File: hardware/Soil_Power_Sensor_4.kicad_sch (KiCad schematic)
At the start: 14 parts, among them J6 UART, SW1 EN, SW2 BOOT, U9 ESP32-C3-WROOM-02-N4

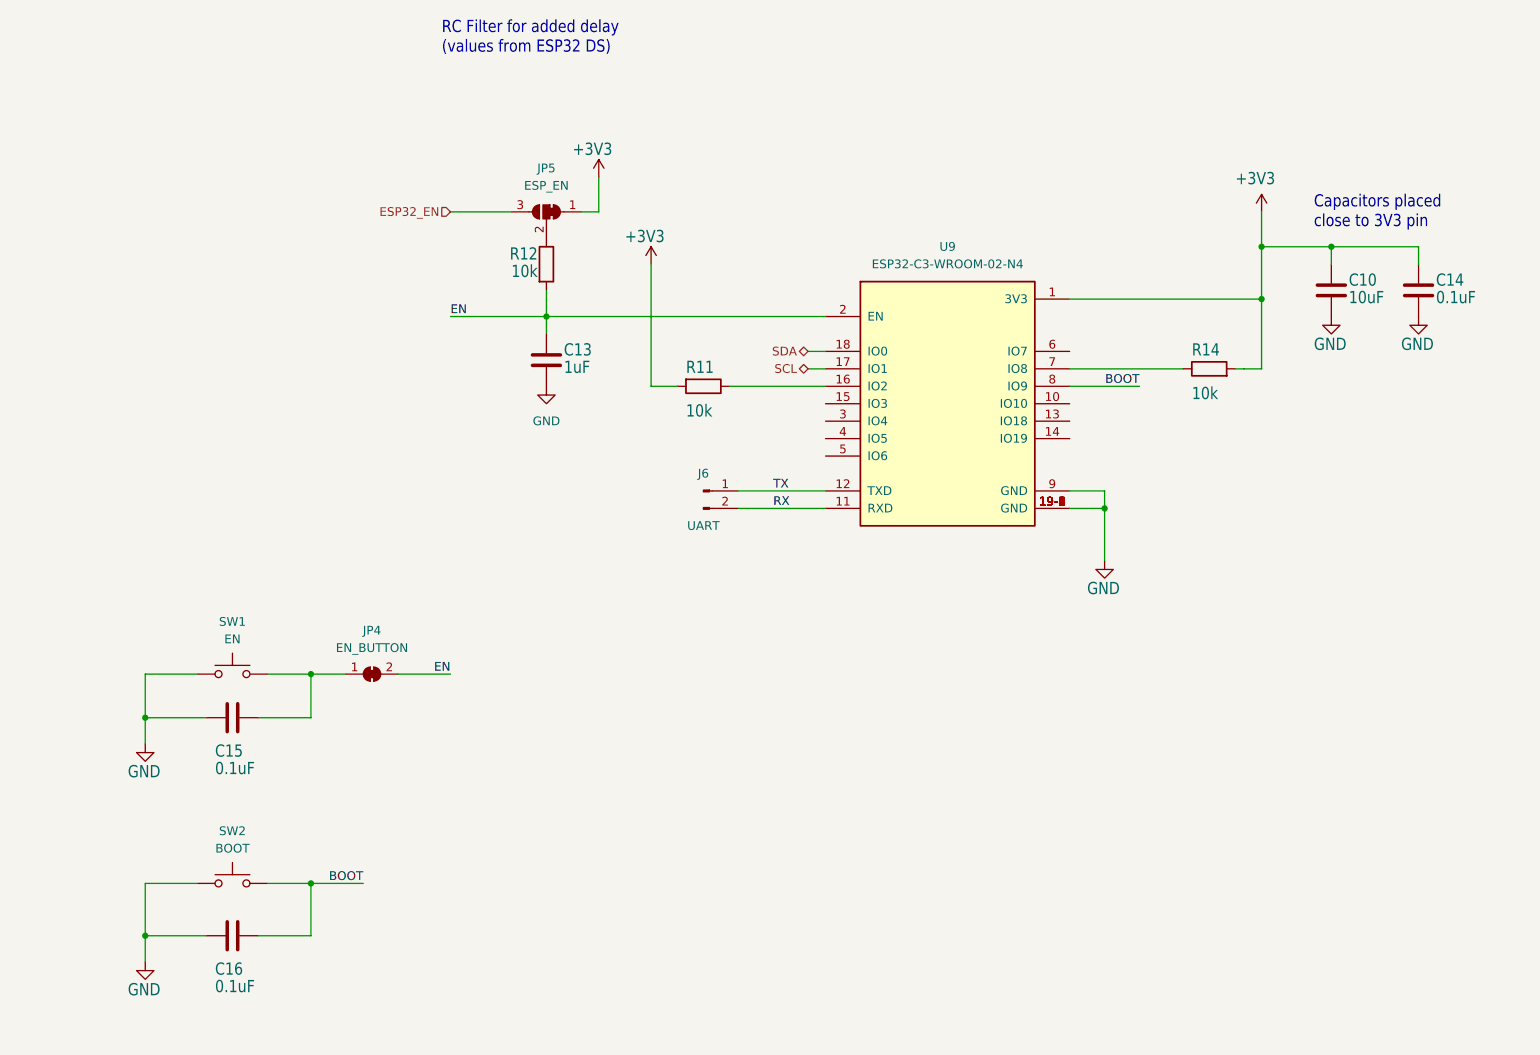
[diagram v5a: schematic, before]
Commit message: Updated annotations based on PCB position
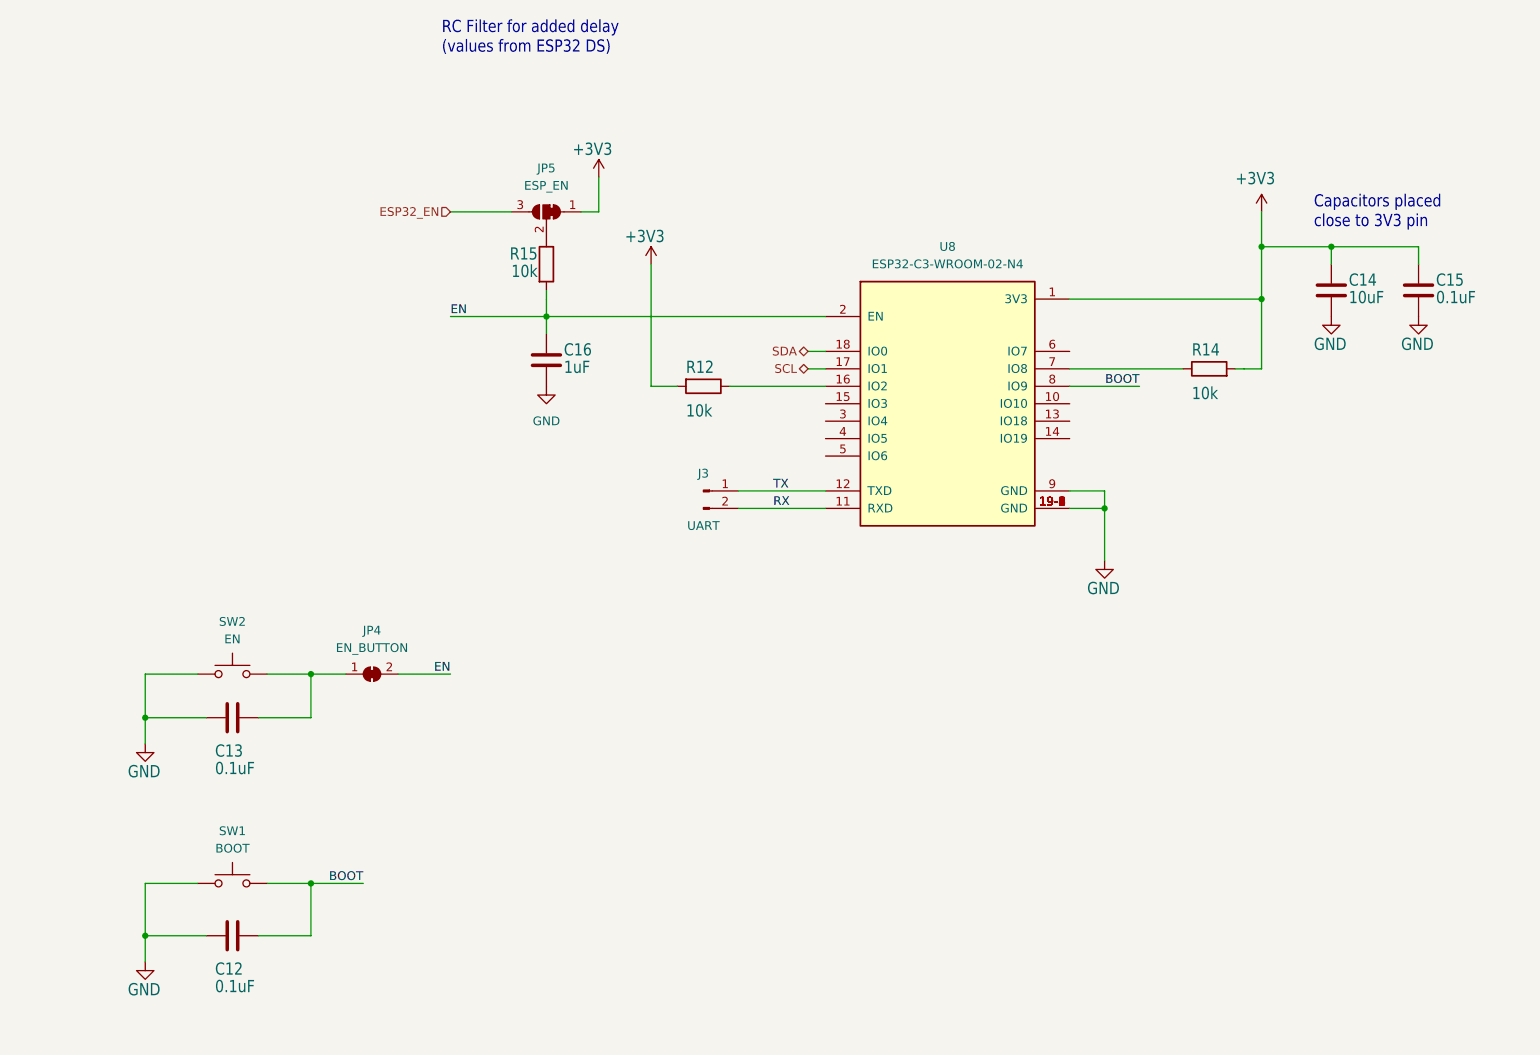
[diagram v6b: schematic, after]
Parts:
- renumbered C16 to C12, C15 to C13, C10 to C14, C14 to C15, C13 to C16, J6 to J3, R11 to R12, R12 to R15, SW2 to SW1, SW1 to SW2, U9 to U8
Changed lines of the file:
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@@
   (title_block
     (title "Soil Power Sensor")
-    (date "2023-10-09")
-    (rev "2.1.0")
+    (date "2024-03-08")
+    (rev "2.2.0")
     (company "jlab")
   )
@@
   (symbol (lib_id "Device:R") (at 129.54 88.9 270) (unit 1)
     (in_bom yes) (on_board yes) (dnp no)
-    (property "Reference" "R11" (at 127 85.09 90)
+    (property "Reference" "R12" (at 127 85.09 90)
       (effects (font (size 1.778 1.5113)) (justify left top))
     )
@@
       (project "Soil Power Sensor"
         (path "/5300ec4d-4648-40a1-8d89-4fa6b3bf32a3/1383843a-880b-4efd-8c7f-ecdf3639f794"
-          (reference "R11") (unit 1)
+          (reference "R12") (unit 1)
         )
       )
@@
   (symbol (lib_id "Device:C") (at 60.96 168.91 270) (unit 1)
     (in_bom yes) (on_board yes) (dnp no)
-    (property "Reference" "C16" (at 58.42 172.72 90)
+    (property "Reference" "C12" (at 58.42 172.72 90)
       (effects (font (size 1.778 1.5113)) (justify left top))
     )
@@
       (project "Soil Power Sensor"
         (path "/5300ec4d-4648-40a1-8d89-4fa6b3bf32a3/1383843a-880b-4efd-8c7f-ecdf3639f794"
-          (reference "C16") (unit 1)
+          (reference "C12") (unit 1)
         )
       )
@@
   (symbol (lib_id "Device:C") (at 106.68 85.09 0) (unit 1)
     (in_bom yes) (on_board yes) (dnp no)
-    (property "Reference" "C13" (at 109.22 82.55 0)
+    (property "Reference" "C16" (at 109.22 82.55 0)
       (effects (font (size 1.778 1.5113)) (justify left top))
     )
@@
       (project "Soil Power Sensor"
         (path "/5300ec4d-4648-40a1-8d89-4fa6b3bf32a3/1383843a-880b-4efd-8c7f-ecdf3639f794"
-          (reference "C13") (unit 1)
+          (reference "C16") (unit 1)
         )
       )
@@
   (symbol (lib_id "Switch:SW_Push") (at 60.96 161.29 0) (unit 1)
     (in_bom yes) (on_board yes) (dnp no) (fields_autoplaced)
-    (property "Reference" "SW2" (at 60.96 153.67 0)
+    (property "Reference" "SW1" (at 60.96 153.67 0)
       (effects (font (size 1.27 1.27)))
     )
@@
       (project "Soil Power Sensor"
         (path "/5300ec4d-4648-40a1-8d89-4fa6b3bf32a3/1383843a-880b-4efd-8c7f-ecdf3639f794"
-          (reference "SW2") (unit 1)
+          (reference "SW1") (unit 1)
         )
       )
@@
   (symbol (lib_id "Device:C") (at 220.98 74.93 0) (unit 1)
     (in_bom yes) (on_board yes) (dnp no)
-    (property "Reference" "C10" (at 223.52 72.39 0)
+    (property "Reference" "C14" (at 223.52 72.39 0)
       (effects (font (size 1.778 1.5113)) (justify left top))
     )
@@
       (project "Soil Power Sensor"
         (path "/5300ec4d-4648-40a1-8d89-4fa6b3bf32a3/1383843a-880b-4efd-8c7f-ecdf3639f794"
-          (reference "C10") (unit 1)
+          (reference "C14") (unit 1)
         )
       )
@@
   (symbol (lib_id "Device:R") (at 106.68 71.12 0) (unit 1)
     (in_bom yes) (on_board yes) (dnp no)
-    (property "Reference" "R12" (at 105.41 68.58 0)
+    (property "Reference" "R15" (at 105.41 68.58 0)
       (effects (font (size 1.778 1.5113)) (justify right top))
     )
@@
       (project "Soil Power Sensor"
         (path "/5300ec4d-4648-40a1-8d89-4fa6b3bf32a3/1383843a-880b-4efd-8c7f-ecdf3639f794"
-          (reference "R12") (unit 1)
+          (reference "R15") (unit 1)
         )
       )
@@
   (symbol (lib_id "Switch:SW_Push") (at 60.96 130.81 0) (unit 1)
     (in_bom yes) (on_board yes) (dnp no) (fields_autoplaced)
-    (property "Reference" "SW1" (at 60.96 123.19 0)
+    (property "Reference" "SW2" (at 60.96 123.19 0)
       (effects (font (size 1.27 1.27)))
     )
@@
       (project "Soil Power Sensor"
         (path "/5300ec4d-4648-40a1-8d89-4fa6b3bf32a3/1383843a-880b-4efd-8c7f-ecdf3639f794"
-          (reference "SW1") (unit 1)
+          (reference "SW2") (unit 1)
         )
       )
@@
   (symbol (lib_id "Soil Power Sensor-eagle-import:ESP32-C3-WROOM-02-N4") (at 165.1 93.98 0) (unit 1)
     (in_bom yes) (on_board yes) (dnp no) (fields_autoplaced)
-    (property "Reference" "U9" (at 165.1 68.58 0)
+    (property "Reference" "U8" (at 165.1 68.58 0)
       (effects (font (size 1.27 1.27)))
     )
@@
       (project "Soil Power Sensor"
         (path "/5300ec4d-4648-40a1-8d89-4fa6b3bf32a3/1383843a-880b-4efd-8c7f-ecdf3639f794"
-          (reference "U9") (unit 1)
+          (reference "U8") (unit 1)
         )
       )
@@
   (symbol (lib_id "Device:C") (at 233.68 74.93 0) (unit 1)
     (in_bom yes) (on_board yes) (dnp no)
-    (property "Reference" "C14" (at 236.22 72.39 0)
+    (property "Reference" "C15" (at 236.22 72.39 0)
       (effects (font (size 1.778 1.5113)) (justify left top))
     )
@@
       (project "Soil Power Sensor"
         (path "/5300ec4d-4648-40a1-8d89-4fa6b3bf32a3/1383843a-880b-4efd-8c7f-ecdf3639f794"
-          (reference "C14") (unit 1)
+          (reference "C15") (unit 1)
         )
       )
@@
   (symbol (lib_id "Connector:Conn_01x02_Pin") (at 129.54 104.14 0) (unit 1)
     (in_bom yes) (on_board yes) (dnp no)
-    (property "Reference" "J6" (at 129.54 101.6 0)
+    (property "Reference" "J3" (at 129.54 101.6 0)
       (effects (font (size 1.27 1.27)))
     )
@@
       (project "Soil Power Sensor"
         (path "/5300ec4d-4648-40a1-8d89-4fa6b3bf32a3/1383843a-880b-4efd-8c7f-ecdf3639f794"
-          (reference "J6") (unit 1)
+          (reference "J3") (unit 1)
         )
       )
@@
   (symbol (lib_id "Device:C") (at 60.96 137.16 270) (unit 1)
     (in_bom yes) (on_board yes) (dnp no)
-    (property "Reference" "C15" (at 58.42 140.97 90)
+    (property "Reference" "C13" (at 58.42 140.97 90)
       (effects (font (size 1.778 1.5113)) (justify left top))
     )
@@
       (project "Soil Power Sensor"
         (path "/5300ec4d-4648-40a1-8d89-4fa6b3bf32a3/1383843a-880b-4efd-8c7f-ecdf3639f794"
-          (reference "C15") (unit 1)
-        )
-      )
+          (reference "C13") (unit 1)
+        )
+      )

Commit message: Generated BOM
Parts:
- SW1, SW2: MPN (none) -> KSC701J LFS
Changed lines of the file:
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@@
+      (effects (font (size 1.27 1.27)) hide)
+    )
+    (property "MPN" "KSC701J LFS" (at 60.96 161.29 0)
       (effects (font (size 1.27 1.27)) hide)
     )
@@
       (effects (font (size 1.27 1.27)) hide)
     )
+    (property "MPN" "KSC701J LFS" (at 60.96 130.81 0)
+      (effects (font (size 1.27 1.27)) hide)
+    )
